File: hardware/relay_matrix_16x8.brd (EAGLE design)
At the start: 203.2 x 304.7 mm, 275 parts, among them J6 CT3151, J7 CT3151, J8 CT3151, U1 TM4C123GH6PMI, U2 CP2102N-A02-GQFN24R, U20 SN74HCS595, U21 SN74HCS595, U22 SN74HCS595, U23 SN74HCS595, U30 LDD-SMHTA304RISITR, U31 LDD-SMHTA304RISITR, U32 LDD-SMHTA304RISITR, U33 LDD-SMHTA304RISITR, U34 LDD-SMHTA304RISITR, U35 LDD-SMHTA304RISITR, U36 LDD-SMHTA304RISITR, U37 LDD-SMHTA304RISITR, U38 LDD-SMHTA304RISITR, U4 TLS835B2ELVSE, U5 TLS835B2ELVSE, X1 2171790001, X101 364A2595, X102 364A2595, X103 364A2595, X104 364A2595, X105 364A2595, X106 364A2595, X107 364A2595, X108 364A2595, X111 364A2595, X112 364A2595, X113 364A2595, X114 364A2595, X2 FTSH-105-01-F-DV-007-K-P, X3 SJ1-3523NG, X4 SJ1-3523NG, X5 SJ1-3523NG

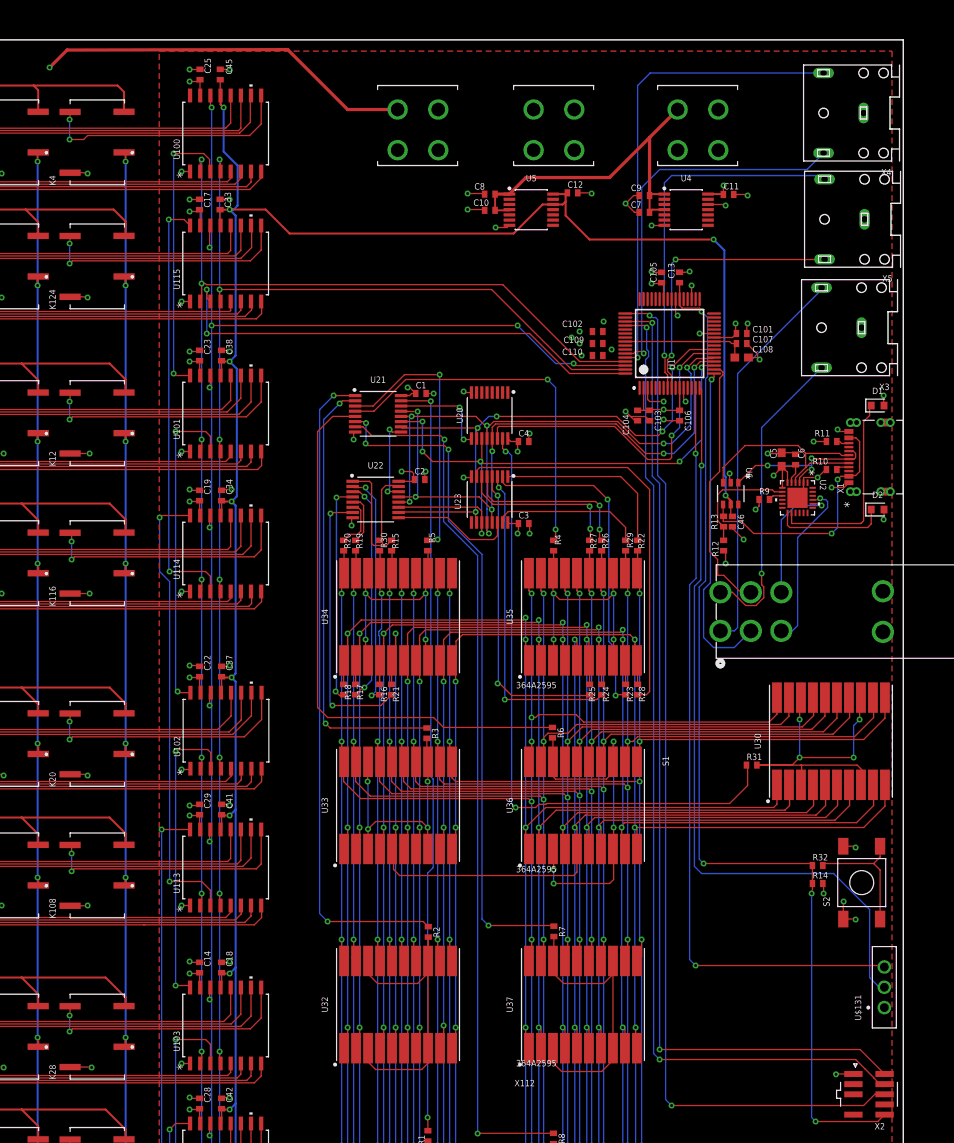
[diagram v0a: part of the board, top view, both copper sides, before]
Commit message: replace LDOs with more common part
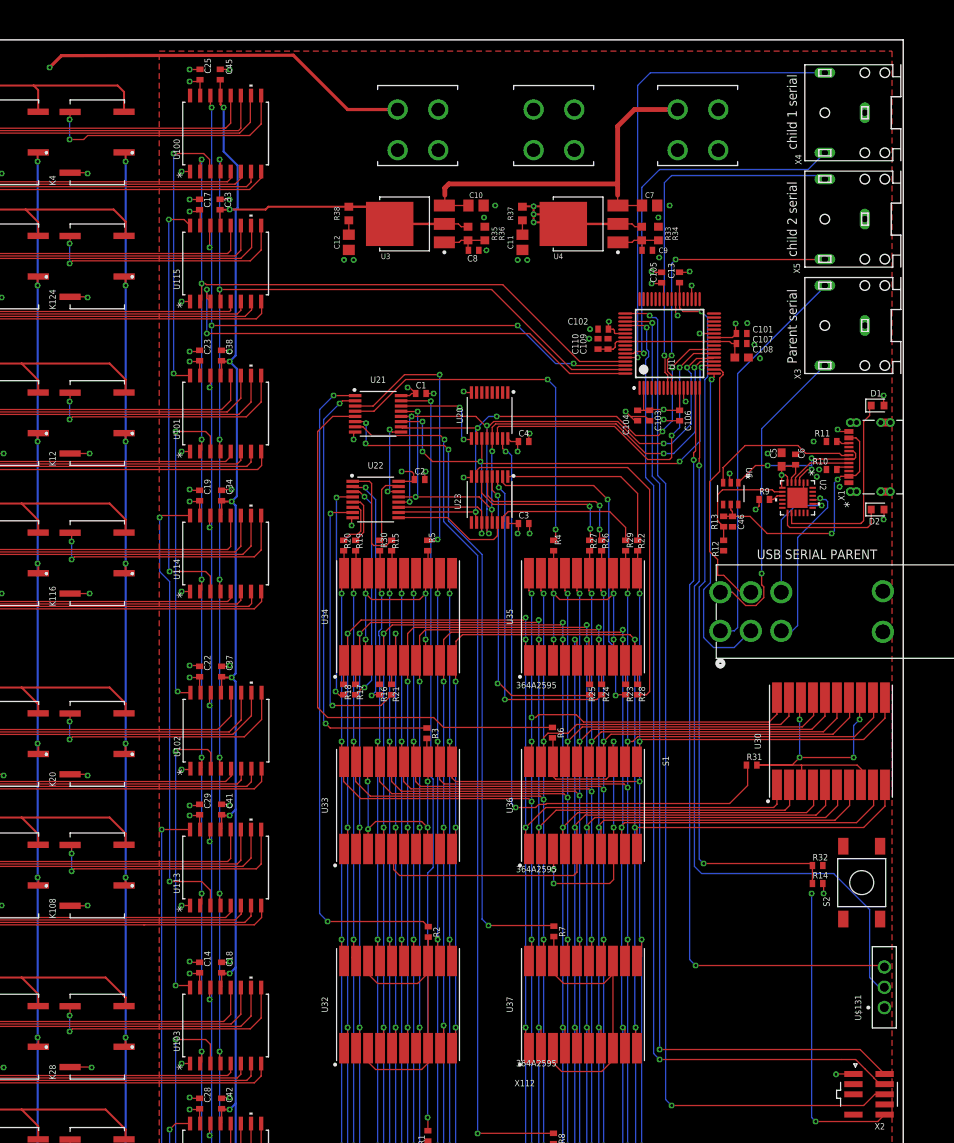
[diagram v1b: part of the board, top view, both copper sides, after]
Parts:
- removed U5: TLS835B2ELVSE, TLS835B2ELVSEXUMA1:SOP65P600X170-14N
- added R33, R35: 220, rcl:R0603
- added R34: 360, rcl:R0603
- added R36: 680, rcl:R0603
- added R37, R38: 1, rcl:R0603
- added U3: NCP1117XXA, 1117:TO230P990X240-4N
- C10, C7: value .1uF -> 10uF; device resistor:C0402 -> rcl:C0805
- C11, C12: value 1uF -> 10uF; device resistor:C0402 -> rcl:C0805
- C8, C9: value .1uF -> 1uF
- U4: value TLS835B2ELVSE -> NCP1117XXA; device TLS835B2ELVSEXUMA1:SOP65P600X170-14N -> 1117:TO230P990X240-4N
- moved C12 28.6 mm to (133.9, 279.4), turned to 270 degrees
- moved C11 26.5 mm to (155.6, 279.4), turned to 270 degrees
- moved U4 12.9 mm to (163.3, 281.7), turned to 180 degrees
- moved C8 7.31 mm to (149.5, 278.4), turned to 0 degrees
- moved C9 6.86 mm to (171.2, 278.4), turned to 0 degrees
- moved C10 1.83 mm to (149.8, 284.0), turned to 0 degrees
- moved C110 1.45 mm to (165.1, 266.7), turned to 90 degrees
- moved C109 1.30 mm to (166.3, 266.7), turned to 90 degrees
- moved C7 1.08 mm to (171.5, 284.0), turned to 0 degrees
- moved C102 0.76 mm to (165.7, 268.6)
- moved X3 0.49 mm to (198.4, 269.0)
- moved X4 0.16 mm to (198.4, 295.6)
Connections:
- net NRESET renamed !RST
- removed net 5V0: C12.1, C18.1, C31.1, C32.1, C33.1, C34.1, C35.1, C36.1, C37.1, C38.1, C39.1, C40.1, C41.1, C42.1, C43.1, C44.1, C45.1, C46.1, U100.13, U101.13, U102.13, U103.13, U104.13, U105.13, U106.13, U107.13, U108.13, U109.13, U110.13, U111.13, U112.13, U113.13, U114.13, U115.13, U5.12, U5.14, U6.5
- removed net VDD: C1.1, C101.1, C102.1, C103.1, C104.1, C105.1, C106.1, C107.1, C108.1, C109.1, C110.1, C14.1, C15.1, C16.1, C17.1, C19.1, C2.1, C20.1, C21.1, C22.1, C23.1, C24.1, C25.1, C26.1, C27.1, C28.1, C29.1, C3.1, C30.1, C4.1, C5.1, C6.1, D1.2, D2.2, R14.2, R9.1, U1.11, U1.2, U1.25, U1.26, U1.42, U1.54, U1.56, U100.15, U101.15, U102.15, U103.15, U104.15, U105.15, U106.15, U107.15, U108.15, U109.15, U110.15, U111.15, U112.15, U113.15, U114.15, U115.15, U2.5, U2.6, U2.7, U20.16, U21.16, U22.16, U23.16, X2.P$1
- new net +5V: C18.1, C31.1, C32.1, C33.1, C34.1, C35.1, C36.1, C37.1, C38.1, C39.1, C40.1, C41.1, C42.1, C43.1, C44.1, C45.1, R35.2, R38.2, U100.13, U101.13, U102.13, U103.13, U104.13, U105.13, U106.13, U107.13, U108.13, U109.13, U110.13, U111.13, U112.13, U113.13, U114.13, U115.13, U3.2, U3.4
- new net N$20: C9.1, R33.1, R34.2, U4.1
- new net N$21: C8.1, R35.1, R36.2, U3.1
- new net N$22: C11.1, R37.1
- new net N$23: C12.1, R38.1
- new net VDDC: C107.1, C108.1, C109.1, C110.1, U1.25, U1.56
- net +12V: now also U3.3, U4.3; no longer C8.1, C9.1, U4.1, U4.4, U5.1, U5.4
- net GND: now also R34.1, R36.1, S2.P$3, S2.P$4, X2.P$9; no longer S2.P$1, S2.P$2, U4.12, U4.7, U5.7
- net N$19: now also S2.P$1, S2.P$2; no longer S2.P$3, S2.P$4
- net VBUS: now also C46.1, U6.5; no longer U6.4
- net VCC: now also C1.1, C101.1, C102.1, C103.1, C104.1, C105.1, C106.1, C14.1, C15.1, C16.1, C17.1, C19.1, C2.1, C20.1, C21.1, C22.1, C23.1, C24.1, C25.1, C26.1, C27.1, C28.1, C29.1, C3.1, C30.1, C4.1, C5.1, C6.1, D1.2, D2.2, R14.2, R33.2, R37.2, R9.1, U1.11, U1.2, U1.26, U1.42, U1.54, U100.15, U101.15, U102.15, U103.15, U104.15, U105.15, U106.15, U107.15, U108.15, U109.15, U110.15, U111.15, U112.15, U113.15, U114.15, U115.15, U2.5, U2.6, U2.7, U20.16, U21.16, U22.16, U23.16, U4.2, U4.4, X2.P$1; no longer C11.1, U4.14
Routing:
- net 5V0: track 444.2 -> 0.00 mm, vias 18 -> 0
- net +5V: track 0.00 -> 370.3 mm, vias 0 -> 16
- net VCC: track 3.08 -> 253.4 mm, vias 1 -> 34
- net VDD: track 247.5 -> 0.00 mm, vias 32 -> 0
- net GND: track 435.4 -> 388.6 mm, vias 218 -> 214
- net VDDC: track 0.00 -> 19.9 mm
- net N$19: track 16.2 -> 0.00 mm
- net N$20: track 0.00 -> 6.43 mm
- net N$21: track 0.00 -> 6.43 mm
- net +12V: track 44.6 -> 48.3 mm
- net N$23: track 0.00 -> 1.80 mm
- net N$22: track 0.00 -> 1.80 mm
- net USB_DN: track 29.1 -> 27.3 mm
- net !RST: track 130.9 -> 129.9 mm
- net AGND: track 47.5 -> 46.9 mm
- added copper zone on layer 2, net VCC
- removed copper zone on layer 2, net VDD
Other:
- board text added: "Parent serial"
- board text added: "USB SERIAL PARENT"
- board text added: "child 1 serial"
- board text added: "child 2 serial"

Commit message: respace connectors; add mounting holes; add labels
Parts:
- moved X102 2.20 mm to (15.0, 246.0)
- moved X104 2.00 mm to (15.0, 170.0)
- moved X108 2.00 mm to (15.0, 18.0)
- moved X114 2.00 mm to (188.0, 133.0)
- moved R12 1.32 mm to (181.0, 242.8), turned to 180 degrees
- moved J7 1.00 mm to (174.0, 296.0)
- moved X105 1.00 mm to (15.0, 132.0)
- moved X106 1.00 mm to (15.0, 94.0)
- moved X107 1.00 mm to (15.0, 56.0)
- moved X113 1.00 mm to (188.0, 95.0)
- moved C46 0.99 mm to (181.0, 244.0), turned to 180 degrees
- moved R13 0.74 mm to (181.0, 245.2), turned to 0 degrees
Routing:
- net N$19: track 0.00 -> 11.7 mm
- net OUT5: track 403.3 -> 412.3 mm
- net IN1: track 127.7 -> 133.2 mm
- net IN7: track 126.8 -> 132.1 mm
- net IN4: track 127.5 -> 131.9 mm
- net IN3: track 127.2 -> 130.2 mm
- net GND: track 388.6 -> 386.5 mm, vias 214 -> 213
- net PAR_TX: track 38.9 -> 40.8 mm
- net OUT4: track 391.8 -> 393.4 mm
- net IN6: track 125.8 -> 127.1 mm
- net IN14: track 127.0 -> 128.1 mm
- net +12V: track 48.3 -> 47.3 mm
- net IN8: track 122.2 -> 121.2 mm
- net IN2: track 124.8 -> 125.7 mm
- net OUT2: track 420.8 -> 420.1 mm
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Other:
- outline, holes or cut-outs redrawn
- board text added: "+12V"
- board text added: "1"
- board text added: "10"
- board text added: "11"
- board text added: "12"
- board text added: "13"
- board text added: "14"
- board text added: "15"
- board text added: "16"
- board text added: "2"
- board text added: "3"
- board text added: "3.5MM JACK PARENT"
- board text added: "4"
- board text added: "5"
- board text added: "6"
- board text added: "7"
- board text added: "8"
- board text added: "9"
- board text added: "AGND"
- board text added: "GND"
- board text added: "Ka Moamoa"
- board text added: "M5 screw"
- board text added: "USB PORT PARENT"
- board text added: "mcu reset"
- board text removed: "USB SERIAL PARENT"

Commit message: version sent to pcbway
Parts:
- added C47: 100n, resistor:C0402
- added U5: ECS-2033-080-AU, ecs-20xx:OSCCC250X200X110N
- moved C46 17.4 mm to (192.4, 257.2), turned to 90 degrees
- moved U6 11.8 mm to (189.8, 256.5), turned to 0 degrees
- moved R12 7.22 mm to (185.8, 248.2), turned to 0 degrees
- moved R13 6.31 mm to (185.8, 249.3)
- moved C5 1.95 mm to (189.9, 252.7), turned to 0 degrees
- moved C6 0.76 mm to (189.9, 251.5), turned to 0 degrees
- moved R9 0.17 mm to (185.8, 247.1)
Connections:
- new net OSC: U1.34, U5.3
- net GND: now also C47.2, U5.2
- net VCC: now also C47.1, U5.1, U5.4
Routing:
- net SER_VBUS: track 15.0 -> 3.93 mm
- net USB_DN: track 27.3 -> 17.3 mm, vias 0 -> 2
- net VBUS: track 31.6 -> 23.4 mm
- net PAR_TX: track 40.8 -> 44.1 mm
- net OSC: track 0.00 -> 2.26 mm
- net VCC: track 253.4 -> 255.1 mm, vias 34 -> 35
- net USB_DP: track 21.1 -> 20.3 mm
- net !RST: track 130.3 -> 131.0 mm
- net GND: vias 213 -> 215
- net MCU_RX_C2: vias 2 -> 1
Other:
- board text added: "M4screw"
- board text added: "debug rx"
- board text added: "debug tx"
- board text removed: "M5 screw"

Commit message: finish filling out part ordering info
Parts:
- C13: value 1nF -> 0.01uF
